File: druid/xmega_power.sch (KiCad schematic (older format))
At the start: 30 parts, among them U3 TP4056, U4 TP4056, U5 XC6206P332MR

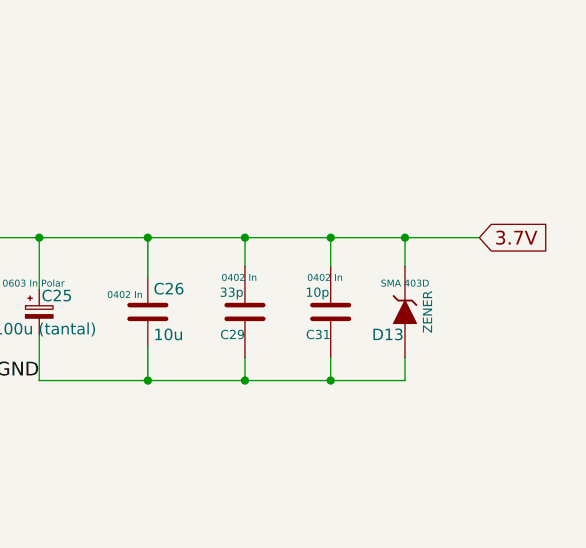
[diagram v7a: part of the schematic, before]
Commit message: Some small fixes. generated net list.
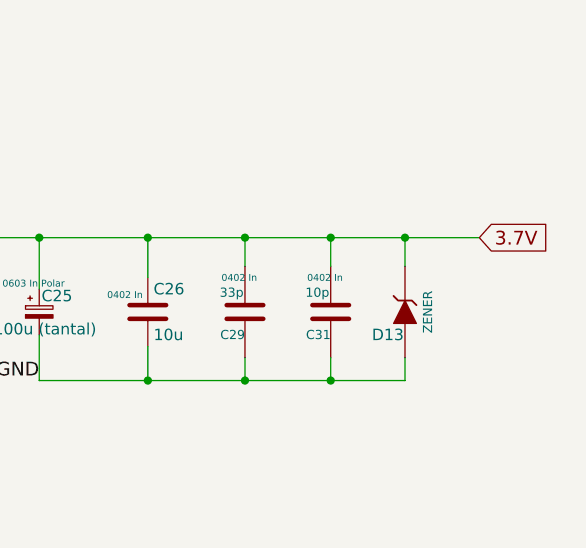
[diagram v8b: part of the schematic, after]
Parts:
- C29: footprint (none) -> Capacitors_SMD:C_0402
- D13: case (none) -> SMA 403D; case  SMA 403D -> (none)
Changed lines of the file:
@@
 F 0 "C29" H 8375 5675 40  0000 L CNN
 F 1 "33p" H 8381 5490 40  0000 L CNN
-F 2 "" H 8413 5425 30  0000 C CNN
+F 2 "Capacitors_SMD:C_0402" H 8413 5425 30  0001 C CNN
 F 3 "https://eu.mouser.com/datasheet/2/212/KEM_C1023_X7R_AUTO_SMD-1093309.pdf" H 8375 5575 60  0001 C CNN
 F 4 "https://eu.mouser.com/ProductDetail/KEMET/C0402C330J9RACAUTO?qs=sGAEpiMZZMs0AnBnWHyRQB295tntAovfdTfJuYu7h0zCBKUrKoz%252bFQ%3d%3d" H 8375 5575 60  0001 C CNN "example"
@@
 F 3 "https://eu.mouser.com/datasheet/2/308/1SMA5913BT3-D-1360201.pdf" H 9075 5575 60  0001 C CNN
 F 4 "https://eu.mouser.com/ProductDetail/ON-Semiconductor/1SMA5918BT3G?qs=sGAEpiMZZMtQ8nqTKtFS%2fJ7m6e1KBCgu1vB5isutOYc%3d" H 9075 5575 60  0001 C CNN "example"
-F 5 "SMA 403D" V 9200 5575 30  0000 C CNN "case "
+F 5 "" V 9200 5575 30  0000 C CNN "case "
+F 6 "SMA 403D" H 0   0   50  0001 C CNN "case"
 	1    9075 5575
 	0    -1   -1   0
